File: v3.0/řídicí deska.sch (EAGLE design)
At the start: 26 parts, among them IC1 MC78M12ACDTG, IC2 AZ1117CD5, Q1 NX3008, Q2 NX3008, Q3 NX3008

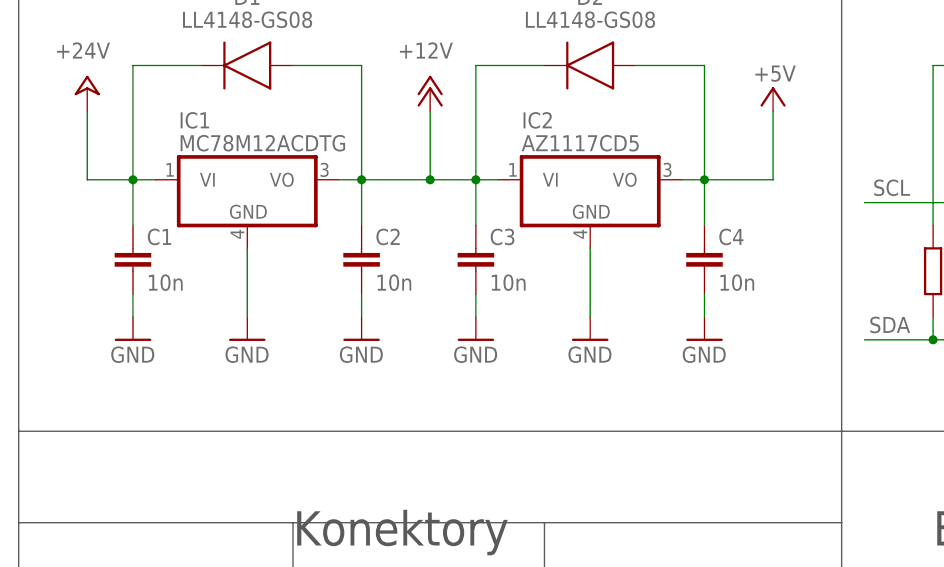
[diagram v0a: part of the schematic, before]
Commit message: přidána rozlévaná měď, rozšířena dokumentace
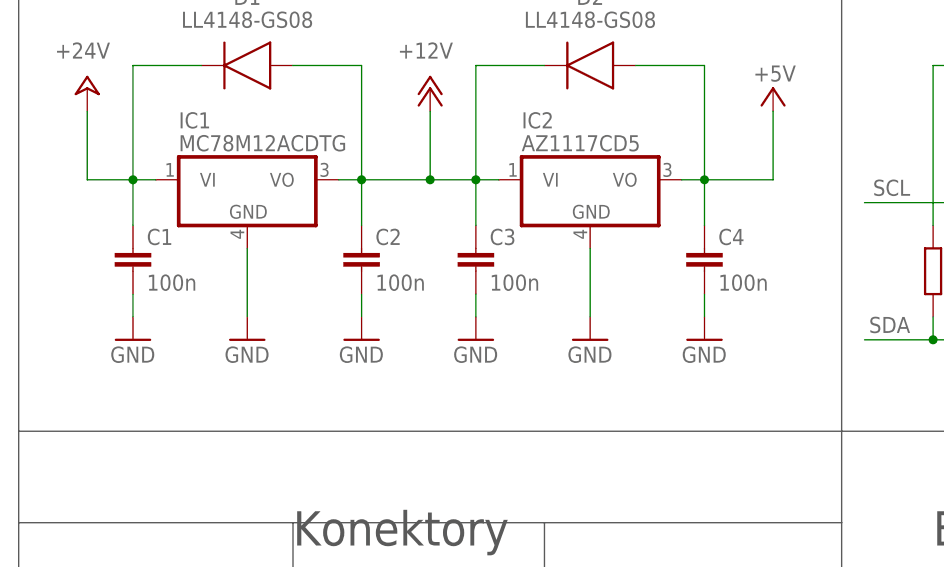
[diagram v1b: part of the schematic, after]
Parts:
- C1, C2, C3, C4: value 10n -> 100n
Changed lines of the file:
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@@
 <part name="IC1" library="linear" library_urn="urn:adsk.eagle:library:262" deviceset="MC78M" device="" package3d_urn="urn:adsk.eagle:package:16495/2" technology="12BDTG" value="MC78M12ACDTG"/>
 <part name="IC2" library="linear" library_urn="urn:adsk.eagle:library:262" deviceset="MC78M" device="" package3d_urn="urn:adsk.eagle:package:16495/2" technology="05CDTG" value="AZ1117CD5"/>
-<part name="C2" library="rcl" library_urn="urn:adsk.eagle:library:334" deviceset="C-EU" device="C0805" package3d_urn="urn:adsk.eagle:package:23617/2" value="10n"/>
-<part name="C3" library="rcl" library_urn="urn:adsk.eagle:library:334" deviceset="C-EU" device="C0805" package3d_urn="urn:adsk.eagle:package:23617/2" value="10n"/>
-<part name="C1" library="rcl" library_urn="urn:adsk.eagle:library:334" deviceset="C-EU" device="C0805" package3d_urn="urn:adsk.eagle:package:23617/2" value="10n"/>
-<part name="C4" library="rcl" library_urn="urn:adsk.eagle:library:334" deviceset="C-EU" device="C0805" package3d_urn="urn:adsk.eagle:package:23617/2" value="10n"/>
+<part name="C2" library="rcl" library_urn="urn:adsk.eagle:library:334" deviceset="C-EU" device="C0805" package3d_urn="urn:adsk.eagle:package:23617/2" value="100n"/>
+<part name="C3" library="rcl" library_urn="urn:adsk.eagle:library:334" deviceset="C-EU" device="C0805" package3d_urn="urn:adsk.eagle:package:23617/2" value="100n"/>
+<part name="C1" library="rcl" library_urn="urn:adsk.eagle:library:334" deviceset="C-EU" device="C0805" package3d_urn="urn:adsk.eagle:package:23617/2" value="100n"/>
+<part name="C4" library="rcl" library_urn="urn:adsk.eagle:library:334" deviceset="C-EU" device="C0805" package3d_urn="urn:adsk.eagle:package:23617/2" value="100n"/>
 <part name="GND3" library="supply1" library_urn="urn:adsk.eagle:library:371" deviceset="GND" device=""/>
 <part name="GND4" library="supply1" library_urn="urn:adsk.eagle:library:371" deviceset="GND" device=""/>

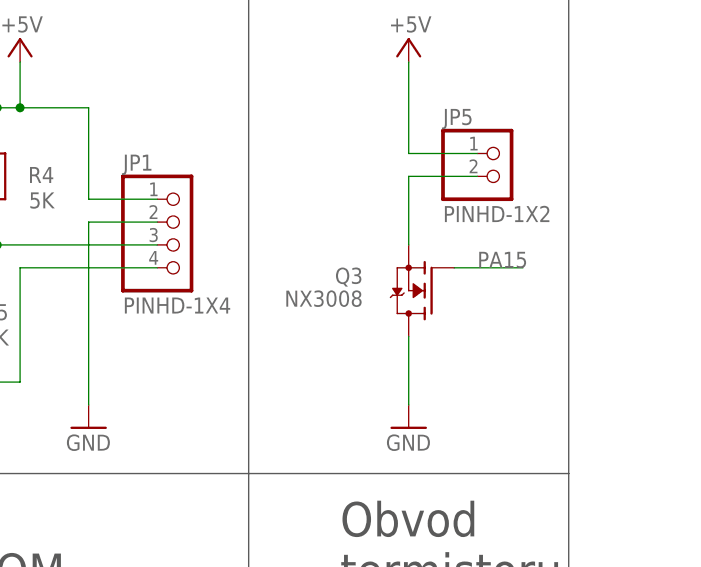
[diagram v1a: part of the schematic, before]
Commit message: oprava mosfet ventilátoru
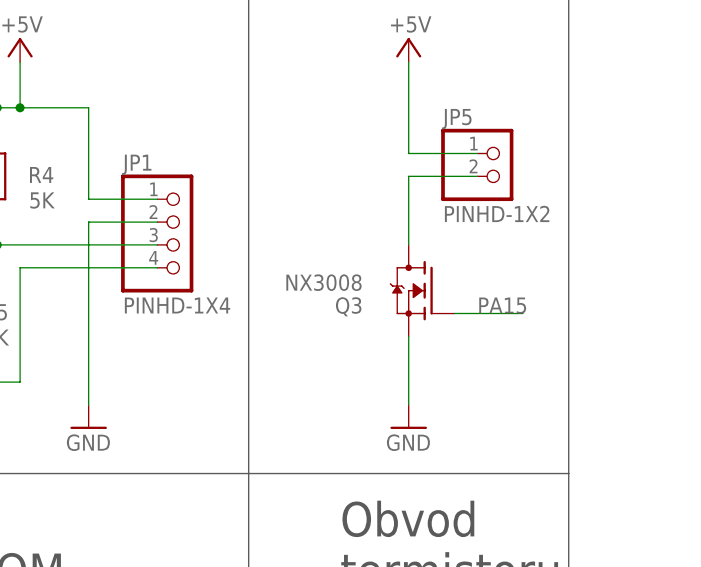
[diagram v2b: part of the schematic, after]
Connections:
- net GND: now also Q3.S; no longer Q3.D
- net N$5: now also Q3.D; no longer Q3.S
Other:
- moved on the sheet: Q3
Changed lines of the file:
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@@
 <?xml version="1.0" encoding="utf-8"?>
 <!DOCTYPE eagle SYSTEM "eagle.dtd">
-<eagle version="9.7.0">
+<eagle version="9.5.1">
 <drawing>
 <settings>
@@
 <attribute name="VALUE" x="182.88" y="40.64" size="1.778" layer="96" rot="R180"/>
 </instance>
-<instance part="Q3" gate="G$1" x="180.34" y="76.2" smashed="yes" rot="R180">
-<attribute name="NAME" x="172.72" y="78.74" size="1.778" layer="95" rot="R180"/>
-<attribute name="VALUE" x="172.72" y="76.2" size="1.778" layer="96" rot="R180"/>
+<instance part="Q3" gate="G$1" x="180.34" y="76.2" smashed="yes" rot="MR0">
+<attribute name="NAME" x="172.72" y="73.66" size="1.778" layer="95" rot="MR0"/>
+<attribute name="VALUE" x="172.72" y="76.2" size="1.778" layer="96" rot="MR0"/>
 </instance>
 <instance part="GND13" gate="1" x="177.8" y="60.96" smashed="yes">
@@
 <pinref part="R1" gate="G$1" pin="1"/>
 <wire x1="180.34" y1="7.62" x2="180.34" y2="12.7" width="0.1524" layer="91"/>
-</segment>
-<segment>
-<pinref part="GND13" gate="1" pin="GND"/>
-<wire x1="177.8" y1="63.5" x2="177.8" y2="71.12" width="0.1524" layer="91"/>
-<pinref part="Q3" gate="G$1" pin="D"/>
 </segment>
 <segment>
@@
 <wire x1="139.7" y1="27.94" x2="129.54" y2="27.94" width="0.1524" layer="91"/>
 <pinref part="U$2" gate="G$1" pin="WC"/>
+</segment>
+<segment>
+<pinref part="GND13" gate="1" pin="GND"/>
+<pinref part="Q3" gate="G$1" pin="S"/>
+<wire x1="177.8" y1="63.5" x2="177.8" y2="71.12" width="0.1524" layer="91"/>
 </segment>
 </net>
@@
 </segment>
 <segment>
-<wire x1="190.5" y1="78.74" x2="182.88" y2="78.74" width="0.1524" layer="91"/>
+<wire x1="190.5" y1="73.66" x2="182.88" y2="73.66" width="0.1524" layer="91"/>
 <pinref part="Q3" gate="G$1" pin="G"/>
-<label x="185.42" y="78.74" size="1.778" layer="95"/>
+<label x="185.42" y="73.66" size="1.778" layer="95"/>
 </segment>
 </net>
 <net name="N$5" class="0">
 <segment>
-<wire x1="177.8" y1="81.28" x2="177.8" y2="88.9" width="0.1524" layer="91"/>
 <wire x1="177.8" y1="88.9" x2="185.42" y2="88.9" width="0.1524" layer="91"/>
 <pinref part="JP5" gate="G$1" pin="2"/>
-<pinref part="Q3" gate="G$1" pin="S"/>
-</segment>
-</net>
+<pinref part="Q3" gate="G$1" pin="D"/>
+<wire x1="177.8" y1="81.28" x2="177.8" y2="88.9" width="0.1524" layer="91"/>
+</segment>
+</net>
